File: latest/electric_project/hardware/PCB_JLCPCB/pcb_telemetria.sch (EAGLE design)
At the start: 39 parts

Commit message: adicao de conexao para pinos extras
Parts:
- added R29, R31: 2.2k, rcl:R-EU_0204/7
- added R30, R32: 3.9k, rcl:R-EU_0204/7
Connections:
- removed net N$5: X1.2
- removed net N$6: X1.1
- removed net N$8: X1.5
- new net EXTRA1: R29.1, X3.2
- new net EXTRA2: R31.2, X1.2
- net 21: now also X1.3
- net 22: now also X1.5, X1.6; no longer X1.3
- net BE_IN: now also X1.1; no longer X1.6
- net C14: now also R31.1, R32.2
- net C15: now also R29.2, R30.1
- net GND: now also R30.2, R32.1
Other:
- note added: "Leituras Digitais Extras"
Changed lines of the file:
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@@
 <part name="R2" library="rcl" library_urn="urn:adsk.eagle:library:334" deviceset="R-EU_" device="0204/7" package3d_urn="urn:adsk.eagle:package:23498/2" value="12k"/>
 <part name="X5" library="con-molex-micro-fit-3_0" deviceset="HEADER_POS6_?" device="43045-0612" override_package3d_urn="urn:adsk.eagle:package:15245787/2" override_package_urn="urn:adsk.eagle:footprint:15245788/1"/>
+<part name="R29" library="rcl" library_urn="urn:adsk.eagle:library:334" deviceset="R-EU_" device="0204/7" package3d_urn="urn:adsk.eagle:package:23498/2" value="2.2k"/>
+<part name="R30" library="rcl" library_urn="urn:adsk.eagle:library:334" deviceset="R-EU_" device="0204/7" package3d_urn="urn:adsk.eagle:package:23498/2" value="3.9k"/>
+<part name="R31" library="rcl" library_urn="urn:adsk.eagle:library:334" deviceset="R-EU_" device="0204/7" package3d_urn="urn:adsk.eagle:package:23498/2" value="2.2k"/>
+<part name="R32" library="rcl" library_urn="urn:adsk.eagle:library:334" deviceset="R-EU_" device="0204/7" package3d_urn="urn:adsk.eagle:package:23498/2" value="3.9k"/>
+<part name="GND9" library="supply1" library_urn="urn:adsk.eagle:library:371" deviceset="GND" device=""/>
 </parts>
 <sheets>
@@
 <frame x1="-13.97" y1="-43.18" x2="26.67" y2="7.62" columns="0" rows="0" layer="91" border-left="no" border-top="no" border-right="no" border-bottom="no"/>
 <text x="-7.62" y="-41.91" size="2.54" layer="91">Leitura Analógica</text>
-<frame x1="-22.86" y1="-49.53" x2="166.37" y2="25.4" columns="0" rows="0" layer="91" border-left="no" border-top="no" border-right="no" border-bottom="no"/>
+<frame x1="-20.32" y1="-49.53" x2="224.79" y2="25.4" columns="0" rows="0" layer="91" border-left="no" border-top="no" border-right="no" border-bottom="no"/>
 <text x="66.548" y="13.716" size="5.08" layer="91">DT's 4</text>
 <frame x1="-96.52" y1="-49.53" x2="-24.13" y2="25.4" columns="0" rows="0" layer="91" border-left="no" border-top="no" border-right="no" border-bottom="no"/>
@@
 <text x="-9.906" y="95.25" size="5.08" layer="91">DT's 2</text>
 <text x="-78.74" y="39.624" size="2.54" layer="91">Leitura Analógica</text>
+<frame x1="165.1" y1="-43.18" x2="218.44" y2="7.62" columns="8" rows="5" layer="91" border-left="no" border-top="no" border-right="no" border-bottom="no"/>
+<text x="173.99" y="-41.91" size="2.54" layer="91">Leituras Digitais Extras</text>
 </plain>
 <instances>
@@
 <attribute name="VALUE" x="-10.16" y="-62.23" size="1.778" layer="96" rot="R90"/>
 <attribute name="NAME" x="-31.242" y="-62.23" size="1.778" layer="95" rot="R90"/>
+</instance>
+<instance part="R29" gate="G$1" x="182.88" y="-6.35" smashed="yes" rot="R180">
+<attribute name="NAME" x="184.404" y="-7.5946" size="1.778" layer="95" rot="R180"/>
+<attribute name="VALUE" x="185.42" y="-3.302" size="1.778" layer="96" rot="R180"/>
+</instance>
+<instance part="R30" gate="G$1" x="177.8" y="-13.97" smashed="yes" rot="R270">
+<attribute name="NAME" x="174.7266" y="-12.446" size="1.778" layer="95" rot="R270"/>
+<attribute name="VALUE" x="179.324" y="-11.43" size="1.778" layer="96" rot="R270"/>
+</instance>
+<instance part="R31" gate="G$1" x="210.82" y="-6.35" smashed="yes">
+<attribute name="NAME" x="209.042" y="-9.4234" size="1.778" layer="95"/>
+<attribute name="VALUE" x="208.788" y="-4.826" size="1.778" layer="96"/>
+</instance>
+<instance part="R32" gate="G$1" x="205.74" y="-13.97" smashed="yes" rot="R90">
+<attribute name="NAME" x="204.4954" y="-16.256" size="1.778" layer="95" rot="R90"/>
+<attribute name="VALUE" x="209.042" y="-16.51" size="1.778" layer="96" rot="R90"/>
+</instance>
+<instance part="GND9" gate="1" x="191.77" y="-34.036" smashed="yes">
+<attribute name="VALUE" x="189.23" y="-36.576" size="1.778" layer="96"/>
 </instance>
 </instances>
@@
 <pinref part="X4" gate="G$1" pin="1"/>
 </segment>
+<segment>
+<pinref part="R30" gate="G$1" pin="2"/>
+<wire x1="177.8" y1="-19.05" x2="177.8" y2="-24.13" width="0.1524" layer="91"/>
+<pinref part="R32" gate="G$1" pin="1"/>
+<wire x1="205.74" y1="-19.05" x2="205.74" y2="-24.13" width="0.1524" layer="91"/>
+<wire x1="177.8" y1="-24.13" x2="191.77" y2="-24.13" width="0.1524" layer="91"/>
+<wire x1="191.77" y1="-24.13" x2="205.74" y2="-24.13" width="0.1524" layer="91"/>
+<wire x1="191.77" y1="-24.13" x2="191.77" y2="-31.496" width="0.1524" layer="91"/>
+<junction x="191.77" y="-24.13"/>
+<pinref part="GND9" gate="1" pin="GND"/>
+</segment>
 </net>
 <net name="22" class="0">
@@
 </segment>
 <segment>
-<wire x1="91.44" y1="-68.58" x2="91.44" y2="-81.28" width="0.1524" layer="91"/>
-<label x="91.44" y="-78.74" size="1.778" layer="95" rot="R90"/>
-<pinref part="X1" gate="G$1" pin="3"/>
-</segment>
-<segment>
 <pinref part="X5" gate="G$1" pin="5"/>
 <wire x1="-17.78" y1="-66.04" x2="-17.78" y2="-71.12" width="0.1524" layer="91"/>
@@
 <pinref part="X5" gate="G$1" pin="4"/>
 </segment>
+<segment>
+<pinref part="X1" gate="G$1" pin="6"/>
+<wire x1="99.06" y1="-68.58" x2="99.06" y2="-81.28" width="0.1524" layer="91"/>
+<label x="99.06" y="-81.28" size="1.778" layer="95" rot="R90"/>
+</segment>
+<segment>
+<pinref part="X1" gate="G$1" pin="5"/>
+<wire x1="96.52" y1="-68.58" x2="96.52" y2="-81.28" width="0.1524" layer="91"/>
+<label x="96.52" y="-81.28" size="1.778" layer="95" rot="R90"/>
+</segment>
 </net>
 <net name="21" class="0">
@@
 </segment>
 <segment>
-<wire x1="93.98" y1="-68.58" x2="93.98" y2="-81.28" width="0.1524" layer="91"/>
-<label x="93.98" y="-78.74" size="1.778" layer="95" rot="R90"/>
-<pinref part="X1" gate="G$1" pin="4"/>
-</segment>
-<segment>
 <wire x1="-25.4" y1="-66.04" x2="-25.4" y2="-72.39" width="0.1524" layer="91"/>
 <label x="-25.908" y="-74.422" size="1.778" layer="95"/>
@@
 <label x="-23.368" y="-76.454" size="1.778" layer="95"/>
 <pinref part="X5" gate="G$1" pin="3"/>
+</segment>
+<segment>
+<pinref part="X1" gate="G$1" pin="4"/>
+<wire x1="93.98" y1="-68.58" x2="93.98" y2="-81.28" width="0.1524" layer="91"/>
+<label x="93.98" y="-81.28" size="1.778" layer="95" rot="R90"/>
+</segment>
+<segment>
+<pinref part="X1" gate="G$1" pin="3"/>
+<wire x1="91.44" y1="-68.58" x2="91.44" y2="-81.28" width="0.1524" layer="91"/>
+<label x="91.44" y="-81.28" size="1.778" layer="95" rot="R90"/>
 </segment>
 </net>
@@
 <label x="17.272" y="112.522" size="1.778" layer="95" rot="R90"/>
 </segment>
+<segment>
+<pinref part="R30" gate="G$1" pin="1"/>
+<pinref part="R29" gate="G$1" pin="2"/>
+<wire x1="177.8" y1="-8.89" x2="177.8" y2="-6.35" width="0.1524" layer="91"/>
+<wire x1="177.8" y1="-6.35" x2="172.212" y2="-6.35" width="0.1524" layer="91"/>
+<label x="172.212" y="-6.35" size="1.778" layer="95"/>
+</segment>
 </net>
 <net name="C14" class="0">
@@
 <wire x1="19.812" y1="120.142" x2="19.812" y2="112.522" width="0.1524" layer="91"/>
 <label x="19.812" y="112.522" size="1.778" layer="95" rot="R90"/>
+</segment>
+<segment>
+<pinref part="R32" gate="G$1" pin="2"/>
+<pinref part="R31" gate="G$1" pin="1"/>
+<wire x1="205.74" y1="-8.89" x2="205.74" y2="-6.35" width="0.1524" layer="91"/>
+<wire x1="205.74" y1="-6.35" x2="200.152" y2="-6.35" width="0.1524" layer="91"/>
+<label x="200.152" y="-6.096" size="1.778" layer="95"/>
 </segment>
 </net>
@@
 </segment>
 <segment>
-<wire x1="99.06" y1="-68.58" x2="99.06" y2="-81.28" width="0.1524" layer="91"/>
-<label x="99.06" y="-78.74" size="1.778" layer="95" rot="R90"/>
-<pinref part="X1" gate="G$1" pin="6"/>
+<wire x1="86.36" y1="-68.58" x2="86.36" y2="-81.28" width="0.1524" layer="91"/>
+<pinref part="X1" gate="G$1" pin="1"/>
+<label x="85.344" y="-80.772" size="1.778" layer="95" rot="R90"/>
 </segment>
 </net>
@@
 </segment>
 </net>
-<net name="N$5" class="0">
+<net name="EXTRA1" class="0">
+<segment>
+<pinref part="R29" gate="G$1" pin="1"/>
+<wire x1="187.96" y1="-6.35" x2="187.96" y2="0" width="0.1524" layer="91"/>
+<label x="190.5" y="-2.54" size="1.778" layer="95" rot="R90"/>
+</segment>
+<segment>
+<pinref part="X3" gate="G$1" pin="2"/>
+<wire x1="-123.952" y1="-67.31" x2="-123.952" y2="-82.296" width="0.1524" layer="91"/>
+<label x="-124.206" y="-90.932" size="1.778" layer="95" rot="R90"/>
+</segment>
+</net>
+<net name="EXTRA2" class="0">
+<segment>
+<pinref part="R31" gate="G$1" pin="2"/>
+<wire x1="215.9" y1="-6.35" x2="215.9" y2="0" width="0.1524" layer="91"/>
+<label x="214.63" y="-2.794" size="1.778" layer="95" rot="R90"/>
+</segment>
 <segment>
 <wire x1="88.9" y1="-68.58" x2="88.9" y2="-81.28" width="0.1524" layer="91"/>
-<label x="88.9" y="-78.74" size="1.778" layer="95" rot="R90"/>
+<label x="88.9" y="-81.28" size="1.778" layer="95" rot="R90"/>
 <pinref part="X1" gate="G$1" pin="2"/>
 </segment>
 </net>
-<net name="N$6" class="0">
-<segment>
-<wire x1="86.36" y1="-68.58" x2="86.36" y2="-81.28" width="0.1524" layer="91"/>
-<label x="86.36" y="-78.74" size="1.778" layer="95" rot="R90"/>
-<pinref part="X1" gate="G$1" pin="1"/>
-</segment>
-</net>
-<net name="N$8" class="0">
-<segment>
-<wire x1="96.52" y1="-68.58" x2="96.52" y2="-81.28" width="0.1524" layer="91"/>
-<label x="96.52" y="-78.74" size="1.778" layer="95" rot="R90"/>
-<pinref part="X1" gate="G$1" pin="5"/>
-</segment>
-</net>

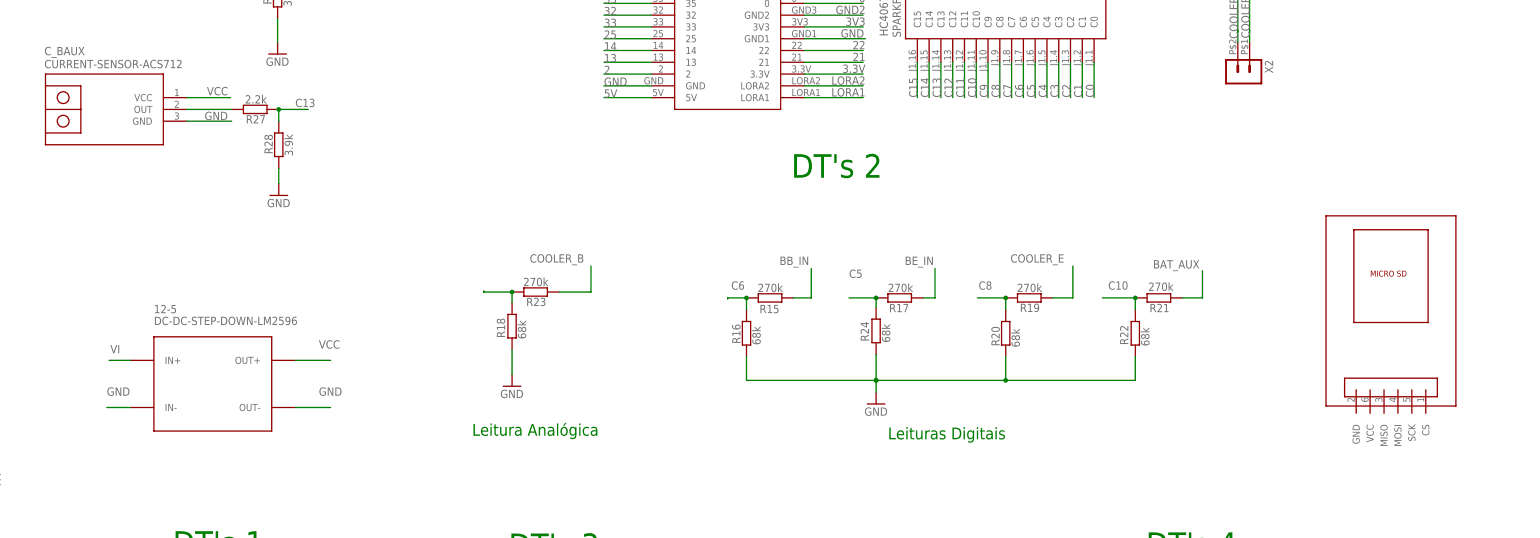
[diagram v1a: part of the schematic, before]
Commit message: adding connector to sd card and capacitors
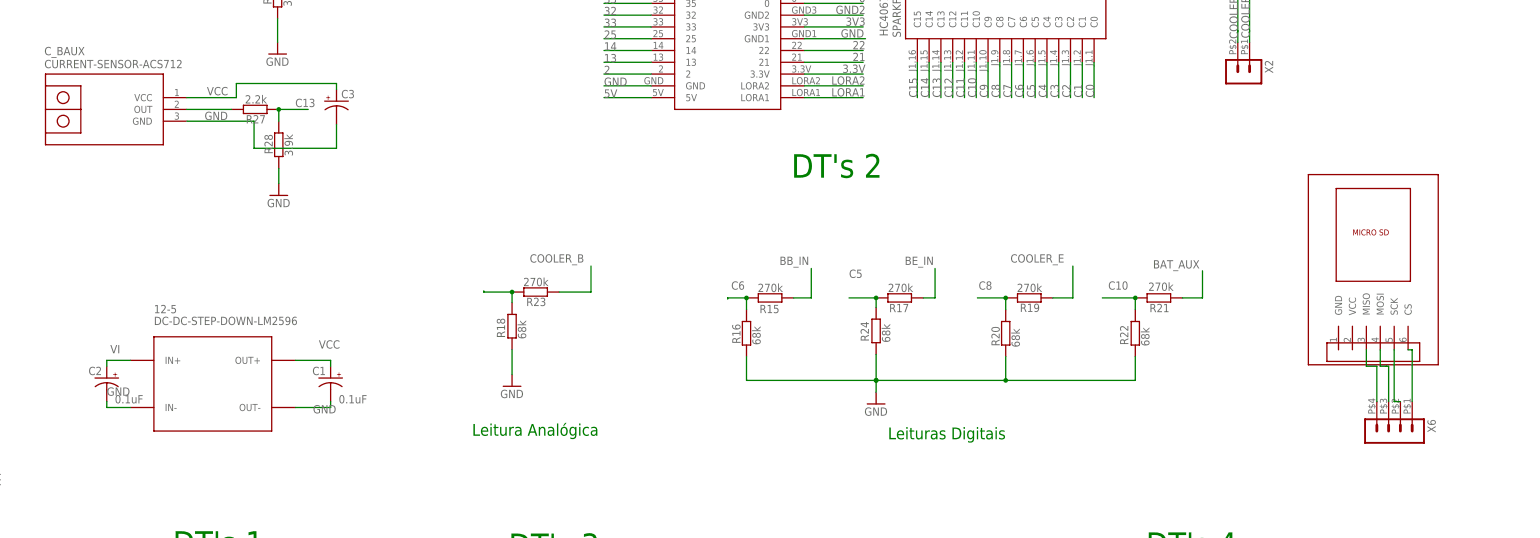
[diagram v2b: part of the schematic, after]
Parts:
- added C1, C2: 0.1uF, rcl:CPOL-USE5-5
- added C3: (no value), rcl:CPOL-USE5-5
- added X6: (no value), con-molex-micro-fit-3_0:HEADER_POS4_43045-0412
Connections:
- new net N$3: U$2.MISO, X6.4
- new net N$4: U$2.MOSI, X6.3
- new net N$6: U$2.CS, X6.1
- new net N$7: U$2.SCK, X6.2
- net GND: now also C1.-, C2.-, C3.-
- net VCC: now also C1.+, C3.+
- net VI: now also C2.+
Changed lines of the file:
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@@
 <?xml version="1.0" encoding="utf-8"?>
 <!DOCTYPE eagle SYSTEM "eagle.dtd">
-<eagle version="9.4.2">
+<eagle version="9.5.0">
 <drawing>
 <settings>
@@
 <setting verticaltext="up"/>
 </settings>
-<grid distance="0.1" unitdist="inch" unit="inch" style="lines" multiple="1" display="no" altdistance="0.01" altunitdist="inch" altunit="inch"/>
+<grid distance="50" unitdist="mil" unit="mil" style="lines" multiple="1" display="no" altdistance="0.01" altunitdist="inch" altunit="inch"/>
 <layers>
 <layer number="1" name="Top" color="4" fill="1" visible="no" active="no"/>
@@
 <part name="GND8" library="supply1" library_urn="urn:adsk.eagle:library:371" deviceset="GND" device=""/>
 <part name="12-5" library="diy-modules" deviceset="DC-DC-STEP-DOWN-LM2596" device="" override_package3d_urn="urn:adsk.eagle:package:15245584/2" override_package_urn="urn:adsk.eagle:footprint:15245585/1"/>
-<part name="U$2" library="bibliotecattgo" deviceset="MICRO_SD_MODULE" device="" override_package3d_urn="urn:adsk.eagle:package:15245275/2" override_package_urn="urn:adsk.eagle:footprint:15245276/1"/>
 <part name="R24" library="rcl" library_urn="urn:adsk.eagle:library:334" deviceset="R-EU_" device="0204/7" package3d_urn="urn:adsk.eagle:package:23498/2" value="68k"/>
 <part name="R18" library="rcl" library_urn="urn:adsk.eagle:library:334" deviceset="R-EU_" device="0204/7" package3d_urn="urn:adsk.eagle:package:23498/2" value="68k"/>
@@
 <part name="R32" library="rcl" library_urn="urn:adsk.eagle:library:334" deviceset="R-EU_" device="0204/7" package3d_urn="urn:adsk.eagle:package:23498/2" value="3.9k"/>
 <part name="GND9" library="supply1" library_urn="urn:adsk.eagle:library:371" deviceset="GND" device=""/>
+<part name="C1" library="rcl" library_urn="urn:adsk.eagle:library:334" deviceset="CPOL-US" device="E5-5" package3d_urn="urn:adsk.eagle:package:23367/2" value="0.1uF"/>
+<part name="C2" library="rcl" library_urn="urn:adsk.eagle:library:334" deviceset="CPOL-US" device="E5-5" package3d_urn="urn:adsk.eagle:package:23367/2" value="0.1uF"/>
+<part name="C3" library="rcl" library_urn="urn:adsk.eagle:library:334" deviceset="CPOL-US" device="E5-5" package3d_urn="urn:adsk.eagle:package:23367/2"/>
+<part name="X6" library="con-molex-micro-fit-3_0" deviceset="HEADER_POS4_?" device="43045-0412" override_package3d_urn="urn:adsk.eagle:package:15245263/2" override_package_urn="urn:adsk.eagle:footprint:15245264/1"/>
+<part name="U$2" library="bibliotecattgo" deviceset="MICRO_SD_MODULE" device=""/>
 </parts>
 <sheets>
@@
 <attribute name="VALUE" x="-147.32" y="63.5" size="1.778" layer="96"/>
 </instance>
-<instance part="U$2" gate="G$1" x="119.38" y="66.04" smashed="yes"/>
 <instance part="R24" gate="G$1" x="8.382" y="62.23" smashed="yes" rot="R270">
 <attribute name="NAME" x="5.0546" y="64.262" size="1.778" layer="95" rot="R270"/>
@@
 <attribute name="VALUE" x="189.23" y="-36.576" size="1.778" layer="96"/>
 </instance>
+<instance part="C1" gate="G$1" x="-109.22" y="52.07" smashed="yes" rot="MR0">
+<attribute name="NAME" x="-110.236" y="52.705" size="1.778" layer="95" rot="MR0"/>
+<attribute name="VALUE" x="-101.346" y="46.609" size="1.778" layer="96" rot="MR0"/>
+</instance>
+<instance part="C2" gate="G$1" x="-157.48" y="52.07" smashed="yes" rot="MR0">
+<attribute name="NAME" x="-158.496" y="52.705" size="1.778" layer="95" rot="MR0"/>
+<attribute name="VALUE" x="-149.606" y="46.609" size="1.778" layer="96" rot="MR0"/>
+</instance>
+<instance part="C3" gate="G$1" x="-107.95" y="111.76" smashed="yes">
+<attribute name="NAME" x="-106.934" y="112.395" size="1.778" layer="95"/>
+<attribute name="VALUE" x="-106.934" y="107.569" size="1.778" layer="96"/>
+</instance>
+<instance part="X6" gate="G$1" x="118.872" y="41.91" smashed="yes" rot="R270">
+<attribute name="VALUE" x="111.252" y="43.18" size="1.778" layer="96" rot="R270"/>
+<attribute name="NAME" x="127.254" y="43.18" size="1.778" layer="95" rot="R270"/>
+</instance>
+<instance part="U$2" gate="G$1" x="115.57" y="74.93" smashed="yes"/>
 </instances>
 <busses>
@@
 <segment>
 <pinref part="C_BAUX" gate="G$1" pin="GND"/>
-<wire x1="-140.208" y1="107.442" x2="-130.556" y2="107.442" width="0.1524" layer="91"/>
+<wire x1="-140.208" y1="107.442" x2="-125.73" y2="107.442" width="0.1524" layer="91"/>
 <label x="-136.398" y="107.696" size="1.778" layer="95"/>
+<wire x1="-125.73" y1="107.442" x2="-125.73" y2="101.6" width="0.1524" layer="91"/>
+<pinref part="C3" gate="G$1" pin="-"/>
+<wire x1="-125.73" y1="101.6" x2="-107.95" y2="101.6" width="0.1524" layer="91"/>
+<wire x1="-107.95" y1="101.6" x2="-107.95" y2="106.68" width="0.1524" layer="91"/>
 </segment>
 <segment>
@@
 <wire x1="-152.4" y1="45.72" x2="-157.48" y2="45.72" width="0.1524" layer="91"/>
 <label x="-157.48" y="48.26" size="1.778" layer="95"/>
+<pinref part="C2" gate="G$1" pin="-"/>
+<wire x1="-157.48" y1="46.99" x2="-157.48" y2="45.72" width="0.1524" layer="91"/>
 </segment>
 <segment>
 <pinref part="12-5" gate="G$1" pin="OUT-"/>
 <wire x1="-116.84" y1="45.72" x2="-109.22" y2="45.72" width="0.1524" layer="91"/>
-<label x="-111.76" y="48.26" size="1.778" layer="95"/>
+<label x="-113.03" y="44.45" size="1.778" layer="95"/>
+<pinref part="C1" gate="G$1" pin="-"/>
+<wire x1="-109.22" y1="46.99" x2="-109.22" y2="45.72" width="0.1524" layer="91"/>
 </segment>
 <segment>
@@
 <segment>
 <pinref part="12-5" gate="G$1" pin="IN+"/>
-<wire x1="-152.4" y1="55.88" x2="-156.972" y2="55.88" width="0.1524" layer="91"/>
+<wire x1="-152.4" y1="55.88" x2="-157.48" y2="55.88" width="0.1524" layer="91"/>
 <label x="-156.718" y="57.404" size="1.778" layer="95"/>
+<pinref part="C2" gate="G$1" pin="+"/>
+<wire x1="-157.48" y1="54.61" x2="-157.48" y2="55.88" width="0.1524" layer="91"/>
 </segment>
 <segment>
@@
 <wire x1="-116.84" y1="55.88" x2="-109.22" y2="55.88" width="0.1524" layer="91"/>
 <label x="-111.76" y="58.42" size="1.778" layer="95"/>
+<pinref part="C1" gate="G$1" pin="+"/>
+<wire x1="-109.22" y1="54.61" x2="-109.22" y2="55.88" width="0.1524" layer="91"/>
 </segment>
 <segment>
 <pinref part="C_BAUX" gate="G$1" pin="VCC"/>
-<wire x1="-140.208" y1="112.522" x2="-130.81" y2="112.522" width="0.1524" layer="91"/>
+<wire x1="-140.208" y1="112.522" x2="-129.54" y2="112.522" width="0.1524" layer="91"/>
 <label x="-135.89" y="113.03" size="1.778" layer="95"/>
+<wire x1="-129.54" y1="112.522" x2="-129.54" y2="115.57" width="0.1524" layer="91"/>
+<wire x1="-129.54" y1="115.57" x2="-107.95" y2="115.57" width="0.1524" layer="91"/>
+<pinref part="C3" gate="G$1" pin="+"/>
+<wire x1="-107.95" y1="115.57" x2="-107.95" y2="114.3" width="0.1524" layer="91"/>
 </segment>
 <segment>
@@
 </segment>
 </net>
+<net name="N$3" class="0">
+<segment>
+<pinref part="X6" gate="G$1" pin="4"/>
+<wire x1="116.332" y1="46.99" x2="116.332" y2="54.61" width="0.1524" layer="91"/>
+<wire x1="116.332" y1="54.61" x2="114.07" y2="54.61" width="0.1524" layer="91"/>
+<pinref part="U$2" gate="G$1" pin="MISO"/>
+<wire x1="114.07" y1="54.61" x2="114.07" y2="58.156" width="0.1524" layer="91"/>
+</segment>
+</net>
+<net name="N$4" class="0">
+<segment>
+<wire x1="118.34" y1="54.61" x2="118.364" y2="54.61" width="0.1524" layer="91"/>
+<pinref part="X6" gate="G$1" pin="3"/>
+<wire x1="118.364" y1="54.61" x2="118.872" y2="54.61" width="0.1524" layer="91"/>
+<wire x1="118.872" y1="54.61" x2="118.872" y2="46.99" width="0.1524" layer="91"/>
+<pinref part="U$2" gate="G$1" pin="MOSI"/>
+<wire x1="117.07" y1="58.156" x2="117.07" y2="54.61" width="0.1524" layer="91"/>
+<wire x1="117.07" y1="54.61" x2="118.34" y2="54.61" width="0.1524" layer="91"/>
+</segment>
+</net>
+<net name="N$7" class="0">
+<segment>
+<pinref part="X6" gate="G$1" pin="2"/>
+<pinref part="U$2" gate="G$1" pin="SCK"/>
+<wire x1="121.412" y1="46.99" x2="120.07" y2="46.99" width="0.1524" layer="91"/>
+<wire x1="120.07" y1="46.99" x2="120.07" y2="58.156" width="0.1524" layer="91"/>
+</segment>
+</net>
+<net name="N$6" class="0">
+<segment>
+<pinref part="X6" gate="G$1" pin="1"/>
+<pinref part="U$2" gate="G$1" pin="CS"/>
+<wire x1="123.952" y1="46.99" x2="123.952" y2="58.156" width="0.1524" layer="91"/>
+<wire x1="123.952" y1="58.156" x2="123.07" y2="58.156" width="0.1524" layer="91"/>
+</segment>
+</net>
